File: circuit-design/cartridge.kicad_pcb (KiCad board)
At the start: 2 copper layers, 43.2 x 39.4 mm, 15 parts, among them J1 Connector, U1 ATmega328P-PU, X1 14.31818MHz

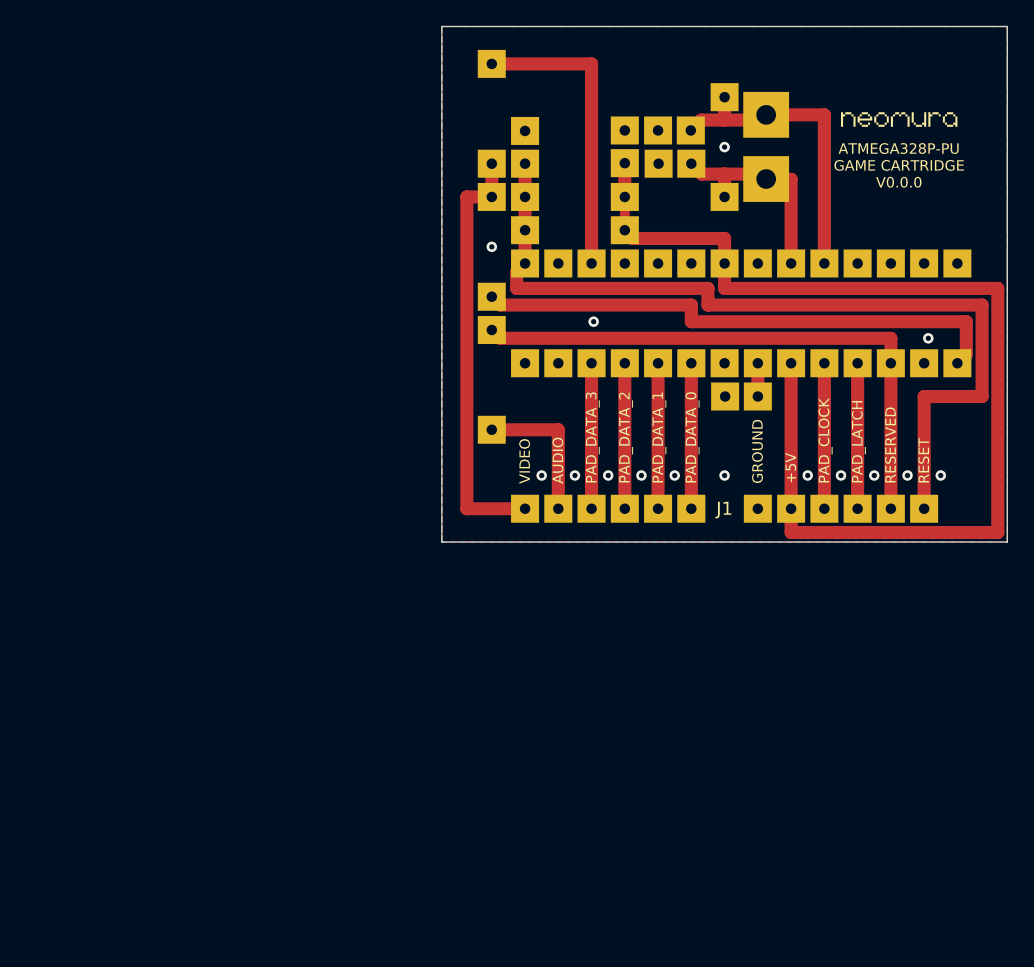
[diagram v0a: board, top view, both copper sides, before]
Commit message: Redesign; uses the new cartridge connector, a smaller crystal, ICSP header, and improved audio.
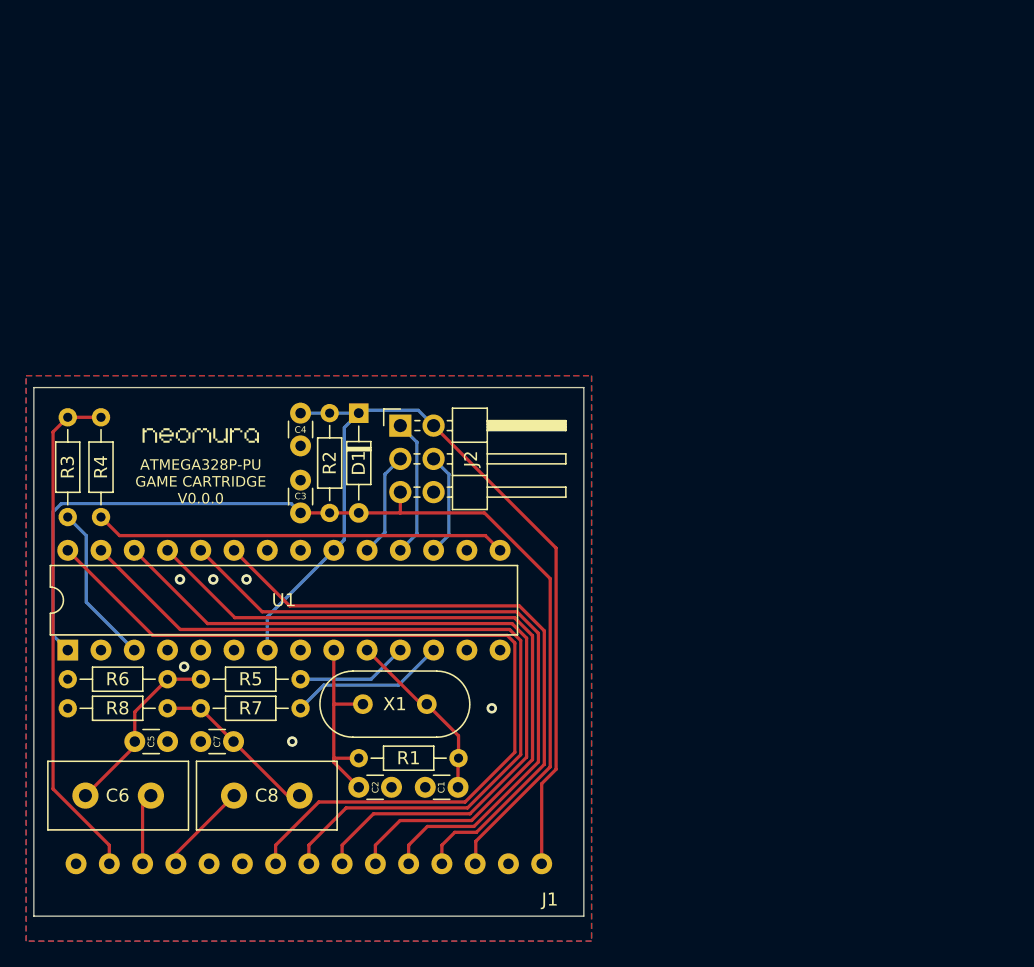
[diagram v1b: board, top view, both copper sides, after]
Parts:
- removed the C4 at (152.4, 110.8)
- added C5: 33n, Capacitor_THT:C_Disc_D3.0mm_W1.6mm_P2.50mm, F.Cu at (107.3, 137.2)
- added C6: 10uF, Capacitor_THT:C_Disc_D10.5mm_W5.0mm_P5.00mm, F.Cu at (106.0, 141.3)
- added C7: 33n, Capacitor_THT:C_Disc_D3.0mm_W1.6mm_P2.50mm, F.Cu at (109.9, 137.2)
- added C8: 10uF, Capacitor_THT:C_Disc_D10.5mm_W5.0mm_P5.00mm, F.Cu at (112.4, 141.3)
- added J2: ICSP, Connector_PinHeader_2.54mm:PinHeader_2x03_P2.54mm_Horizontal, F.Cu at (125.1, 113.0)
- added R6: 150R, Resistor_THT:R_Axial_DIN0204_L3.6mm_D1.6mm_P7.62mm_Horizontal, F.Cu at (107.3, 132.4)
- added R7: 270R, Resistor_THT:R_Axial_DIN0204_L3.6mm_D1.6mm_P7.62mm_Horizontal, F.Cu at (109.9, 134.6)
- added R8: 150R, Resistor_THT:R_Axial_DIN0204_L3.6mm_D1.6mm_P7.62mm_Horizontal, F.Cu at (107.3, 134.6)
- C1, C2, C3, D1, R1, R2, R3, R4, U1: moved to F.Cu
- C4: renamed from C5; moved to F.Cu
- R5: value 100K -> 270R; moved to F.Cu
- X1: footprint Crystal:Crystal_HC50_Horizontal -> Crystal:Crystal_HC49-4H_Vertical; moved to F.Cu
- moved Ref** 58.5 mm to (109.9, 113.8)
- moved R1 54.4 mm to (129.5, 138.4), turned to 180 degrees
- moved C2 54.0 mm to (121.9, 140.7), turned to 0 degrees
- moved C1 53.2 mm to (127.0, 140.7)
- moved X1 51.9 mm to (127.1, 134.3), turned to 180 degrees
- moved R3 47.4 mm to (99.7, 120.0), turned to 90 degrees
- moved U1 45.7 mm to (99.7, 130.2), turned to 90 degrees
- moved J1 42.7 mm to (118.1, 150.5)
- moved R5 34.7 mm to (109.9, 132.4), turned to 0 degrees
- moved R4 34.3 mm to (102.2, 112.4)
- moved C3 31.7 mm to (117.5, 119.7)
- moved C4 31.3 mm to (117.5, 112.1), turned to 270 degrees
- moved R2 27.9 mm to (119.7, 112.1), turned to 270 degrees
- moved D1 24.7 mm to (121.9, 112.1), turned to 270 degrees
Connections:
- J1 pad 1: VIDEO -> GND
- J1 pad 10: MISO_PAD_LATCH -> PAD_1_DATA
- J1 pad 11: MOSI_AUDIO -> PAD_2_DATA
- J1 pad 12: RESET -> PAD_3_DATA
- J1 pad 2: AUDIO -> VIDEO
- J1 pad 3: PAD_3_DATA -> AUDIO_L
- J1 pad 4: PAD_2_DATA -> AUDIO_R
- J1 pad 5: PAD_1_DATA -> Net-(J1-Pad5)
- J1 pad 6: PAD_0_DATA -> Net-(J1-Pad6)
- J1 pad 7: GND -> PAD_LATCH
- J1 pad 8: +5V -> PAD_CLOCK
- J1 pad 9: SCK_PAD_CLOCK -> PAD_0_DATA
- R5 pad 1: MOSI_AUDIO -> Net-(C5-Pad2)
- R5 pad 2: AUDIO -> AUDIO_PWM_L
- U1 pad 11: Net-(U1-Pad11) -> AUDIO_PWM_L
- U1 pad 12: Net-(U1-Pad12) -> AUDIO_PWM_R
- U1 pad 17: MOSI_AUDIO -> MOSI
- U1 pad 18: MISO_PAD_LATCH -> MISO
- U1 pad 19: SCK_PAD_CLOCK -> SCK
- U1 pad 21: AREF -> Net-(U1-Pad21)
- U1 pad 23: PAD_0_DATA -> PAD_3_DATA
- U1 pad 24: PAD_1_DATA -> PAD_2_DATA
- U1 pad 25: PAD_2_DATA -> PAD_1_DATA
- U1 pad 26: PAD_3_DATA -> PAD_0_DATA
- U1 pad 27: Net-(U1-Pad27) -> PAD_CLOCK
- U1 pad 28: Net-(U1-Pad28) -> PAD_LATCH
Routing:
- net PAD_LATCH: track 0.00 -> 68.1 mm
- net PAD_CLOCK: track 0.00 -> 64.1 mm
- net PAD_0_DATA: track 11.1 -> 60.1 mm
- net PAD_1_DATA: track 11.1 -> 56.2 mm
- net MOSI_AUDIO: track 43.8 -> 0.00 mm
- net PAD_2_DATA: track 11.1 -> 52.2 mm
- net PAD_3_DATA: track 11.1 -> 48.2 mm
- net +5V: track 85.0 -> 69.5 mm
- net Net-(C5-Pad2): track 0.00 -> 14.0 mm
- net Net-(C7-Pad2): track 0.00 -> 12.9 mm
- net AUDIO_PWM_R: track 0.00 -> 12.0 mm
- net XTAL2: track 25.5 -> 13.6 mm
- net SCK_PAD_CLOCK: track 11.1 -> 0.00 mm
- net MISO_PAD_LATCH: track 11.1 -> 0.00 mm
- net AUDIO: track 11.1 -> 0.00 mm
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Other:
- board size 43.2 x 39.4 mm -> 42 x 40.4 mm
- net class Default: trace_width 1 -> 0.25

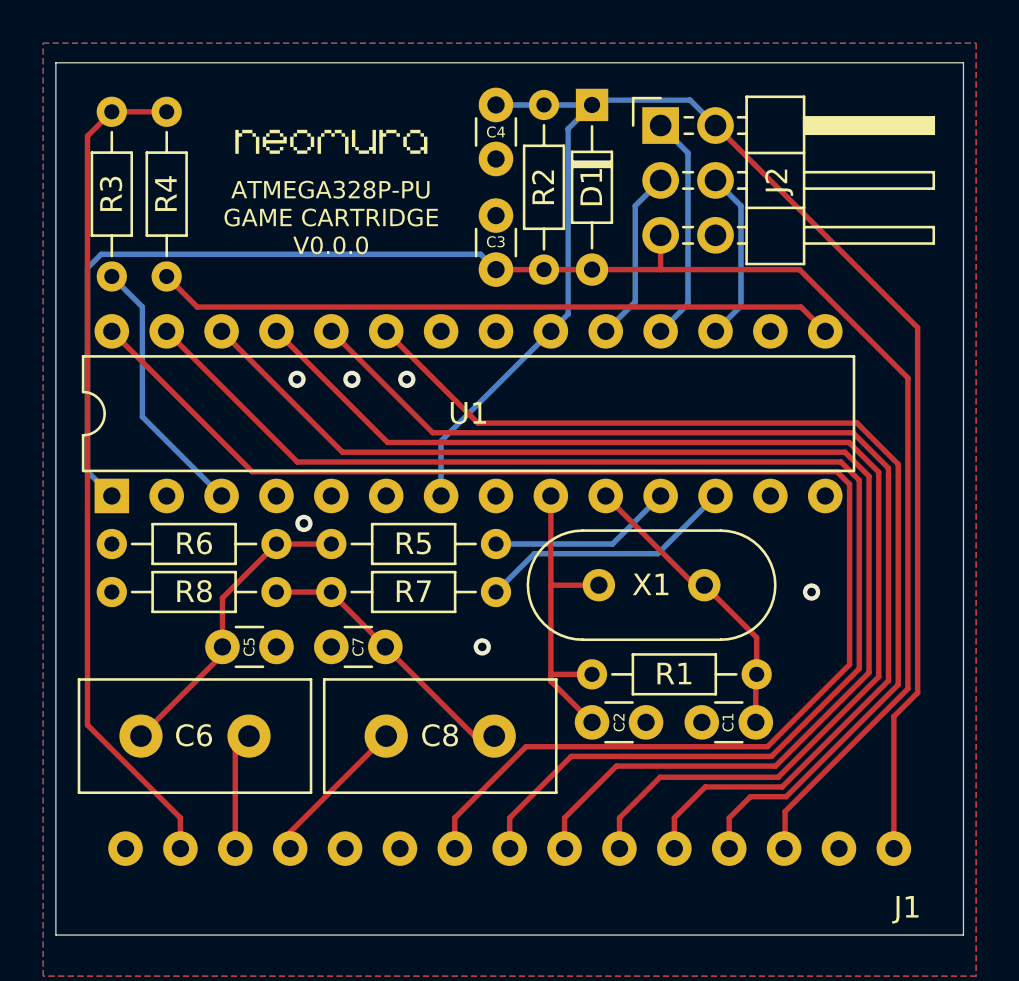
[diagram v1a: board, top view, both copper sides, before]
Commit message: Measure real components and update schematic/PCB layout to match.  This version was sent to prototype manufacturing.
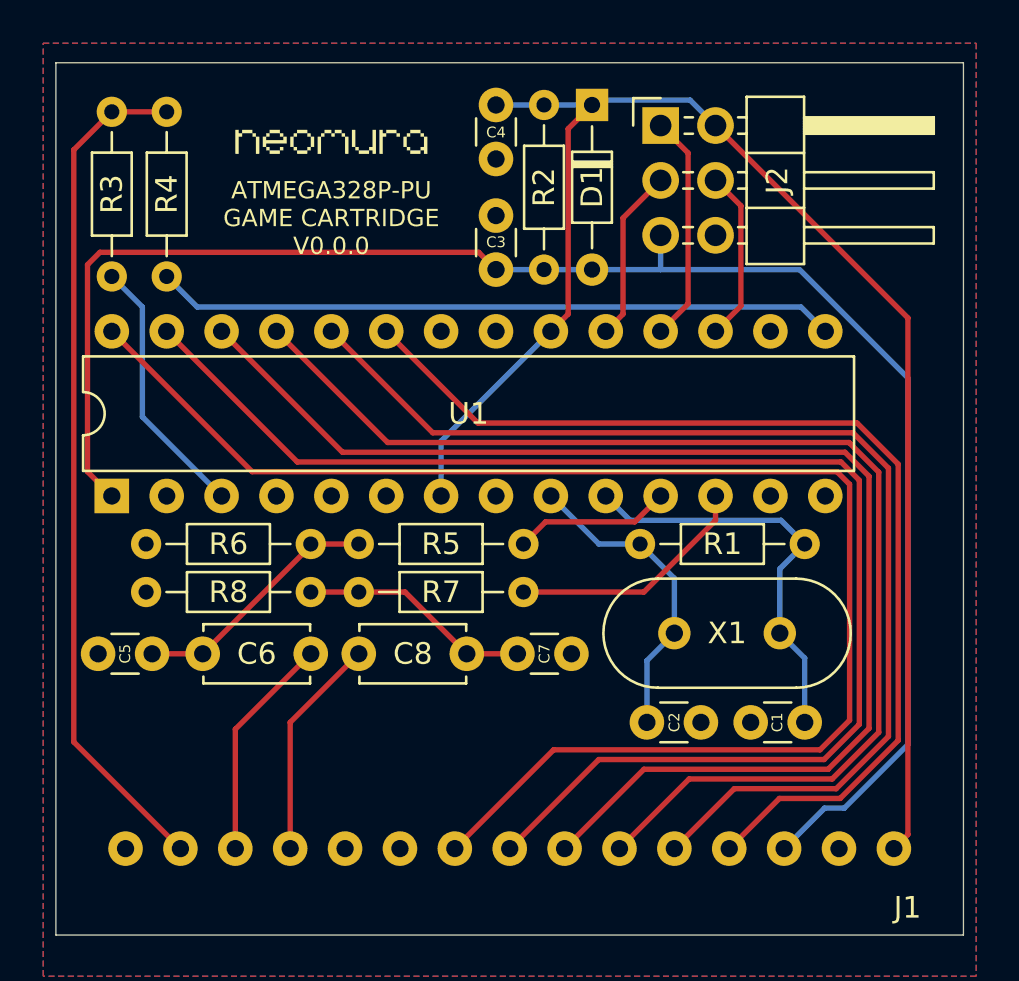
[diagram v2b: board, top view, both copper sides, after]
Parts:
- C6, C8: footprint Capacitor_THT:C_Disc_D10.5mm_W5.0mm_P5.00mm -> Capacitor_THT:C_Disc_D4.7mm_W2.5mm_P5.00mm
- moved C7 11.1 mm to (121.0, 137.5), turned to 180 degrees
- moved C5 8.26 mm to (99.1, 137.5), turned to 0 degrees
- moved R1 6.43 mm to (131.8, 132.4)
- moved C6 4.76 mm to (108.9, 137.5)
- moved X1 4.14 mm to (130.6, 136.5)
- moved C8 4.02 mm to (111.1, 137.5)
- moved C2 2.54 mm to (124.5, 140.7)
- moved C1 2.26 mm to (129.3, 140.7)
- moved R6 1.59 mm to (108.9, 132.4)
- moved R8 1.59 mm to (108.9, 134.6)
- moved R5 1.27 mm to (111.1, 132.4)
- moved R7 1.27 mm to (111.1, 134.6)
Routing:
- net XTAL2: track 13.6 -> 19.3 mm
- net AUDIO_L: track 5.47 -> 10.5 mm
- net AUDIO_R: track 7.05 -> 10.3 mm
- net Net-(C5-Pad2): track 14.0 -> 11.7 mm
- net Net-(C7-Pad2): track 12.9 -> 10.7 mm
- net AUDIO_PWM_L: track 8.54 -> 7.27 mm
- net XTAL1: track 15.4 -> 14.5 mm
- net RESET: track 77.4 -> 78.1 mm
- net PAD_3_DATA: track 48.2 -> 48.9 mm
- net PAD_2_DATA: track 52.2 -> 52.9 mm
- net PAD_LATCH: track 68.1 -> 68.7 mm
- net PAD_CLOCK: track 64.1 -> 64.8 mm
- net PAD_1_DATA: track 56.2 -> 56.8 mm
- net PAD_0_DATA: track 60.1 -> 60.8 mm
- net AUDIO_PWM_R: track 12.0 -> 11.4 mm
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
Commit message: Revise circuit design to remove (potentially dangerous) ICSP VCC pin and remove the need for an adapter to an Arduino.
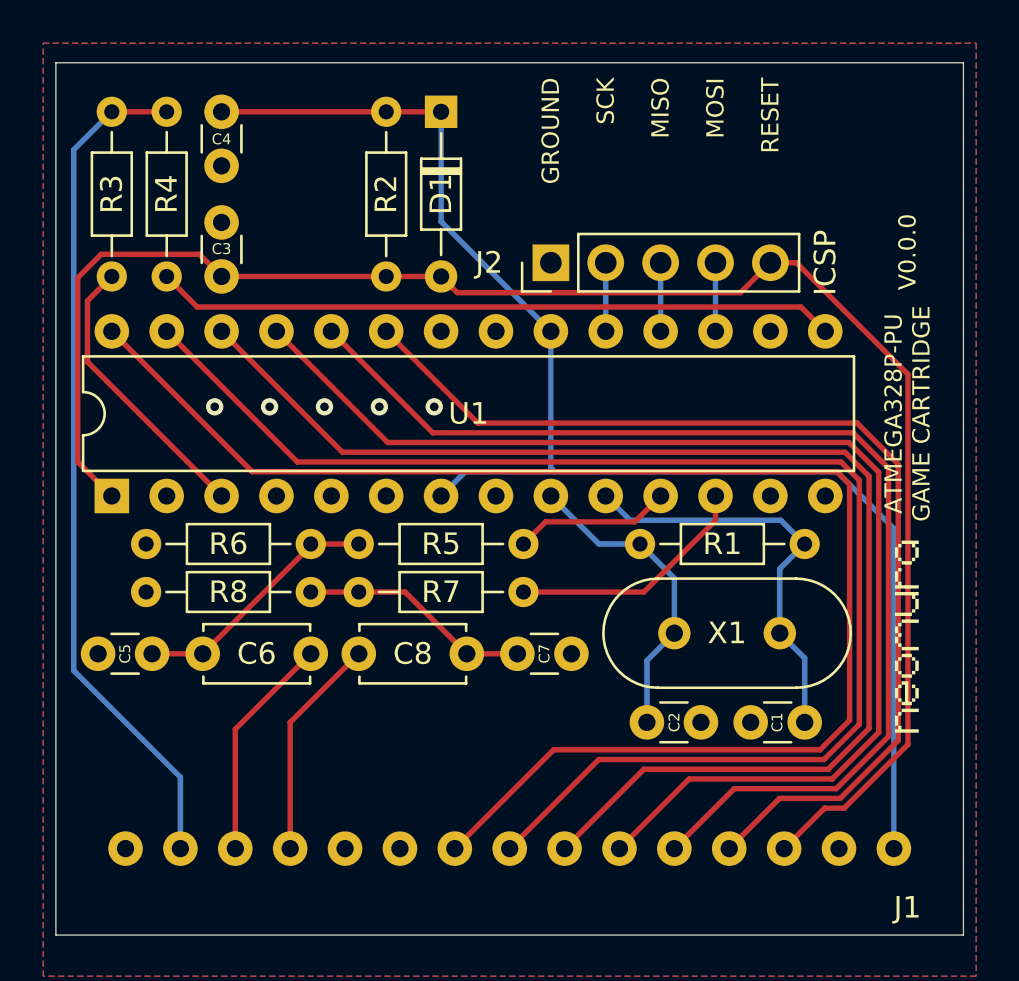
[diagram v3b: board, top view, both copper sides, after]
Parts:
- J2: footprint Connector_PinHeader_2.54mm:PinHeader_2x03_P2.54mm_Horizontal -> Connector_PinHeader_2.54mm:PinHeader_1x05_P2.54mm_Vertical
- X1: value 14.31818MHz -> 14.31818MHz (NTSC) or 17.734MHz (PAL 60)
- moved Ref** 35.1 mm to (136.5, 136.7), turned to 90 degrees
- moved C3 12.7 mm to (104.8, 120.0)
- moved C4 12.7 mm to (104.8, 112.4)
- moved J2 8.13 mm to (120.0, 119.4), turned to 90 degrees
- moved R2 7.31 mm to (112.4, 112.4)
- moved D1 6.99 mm to (114.9, 112.4)
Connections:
- J2 pad 1: MISO -> GND
- J2 pad 2: +5V -> SCK
- J2 pad 3: SCK -> MISO
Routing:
- net MISO: track 10.6 -> 3.18 mm
- net SCK: track 8.04 -> 3.18 mm
- net MOSI: track 7.96 -> 3.18 mm
- net +5V: track 69.2 -> 66.3 mm
- net VIDEO_CARRIER: track 12.3 -> 13.2 mm
- net RESET: track 78.1 -> 78.7 mm
- net GND: vias 0 -> 5
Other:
- board text added: "ATMEGA328P-PU GAME CARTRIDGE"
- board text added: "GROUND"
- board text added: "MISO"
- board text added: "MOSI"
- board text added: "RESET"
- board text added: "SCK"
- board text added: "V0.0.0"
- board text removed: "ATMEGA328P-PU GAME CARTRIDGE V0.0.0"
